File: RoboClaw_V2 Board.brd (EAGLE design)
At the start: 51.8 x 24.4 mm, 11 parts

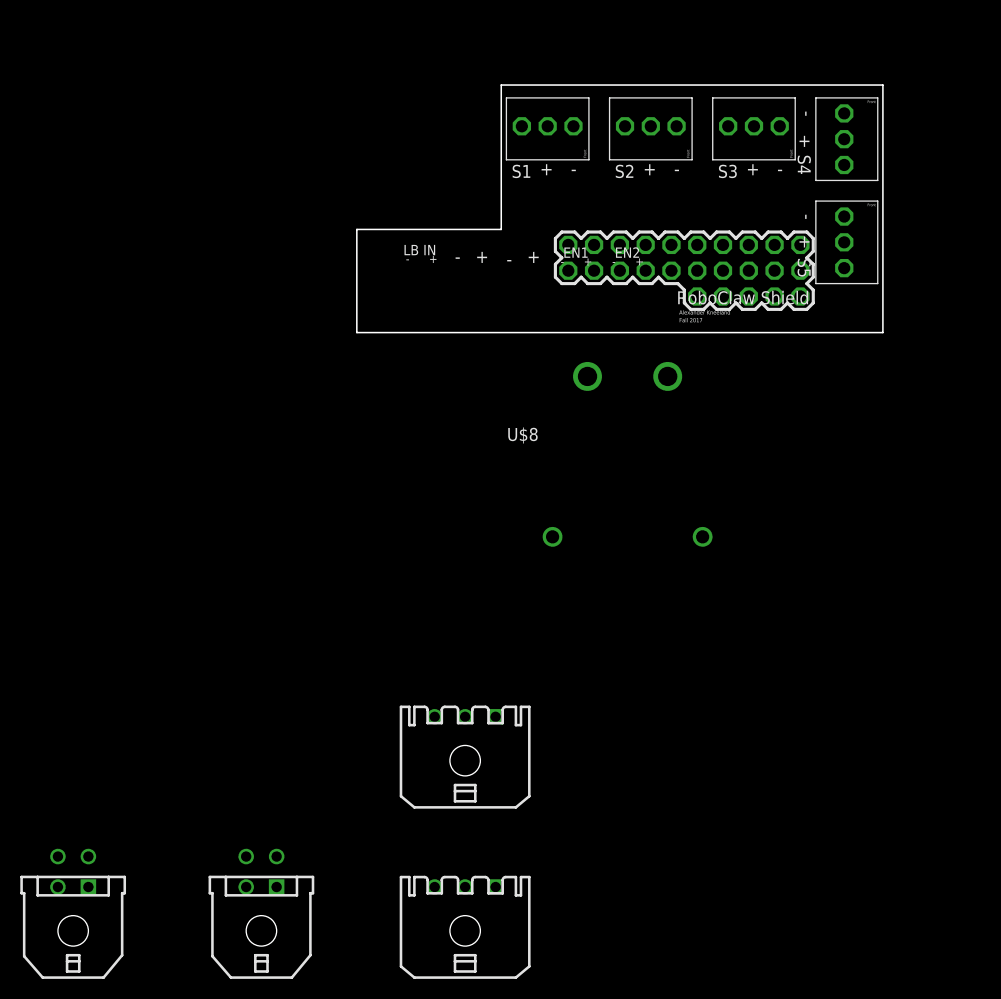
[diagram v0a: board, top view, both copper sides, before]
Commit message: Wired the schematic. Placed and wired the board. First Draft
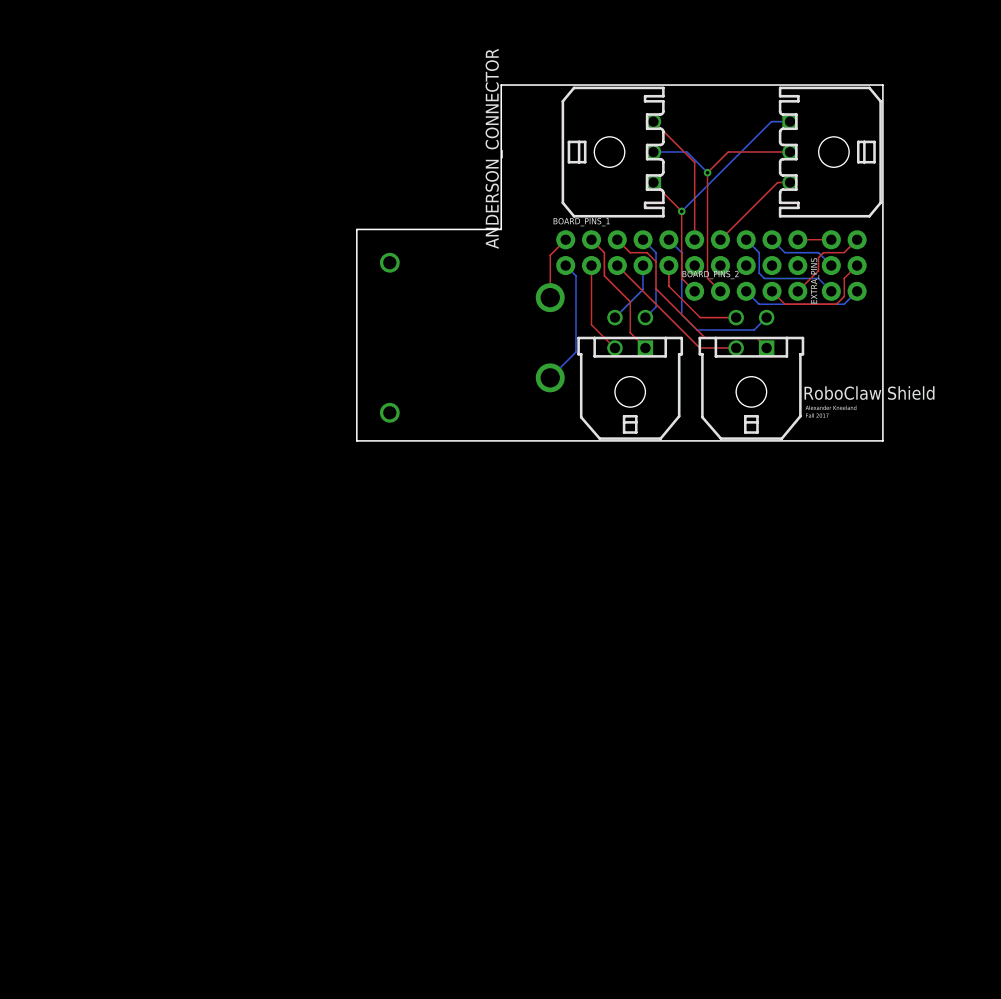
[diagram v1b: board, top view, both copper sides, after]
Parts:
- removed U$1: ROBOCLAW_PINS, Screw Blocks:ROBOCLAW_PINS
- removed U$3, U$4, U$5, U$6, U$7: (no value), Screw Blocks:3_PIN
- removed U$8: (no value), 000_CustomPartsMaster:ANDERSON_RIGHTANGLE_X2
- removed X1, X2: (no value), con-molex-micro-fit-3_0:43650-0300
- removed X3, X4: (no value), con-molex-micro-fit-3_0:43045-0400
- added ANDERSON_CONNECTOR: (no value), 000_CustomPartsMaster:ANDERSON_RIGHTANGLE_X2
- added BOARD_PINS_1: (no value), SparkFun-Connectors:2X10_NOSILK
- added BOARD_PINS_2: (no value), SparkFun-Connectors:1X05_NO_SILK
- added ENCODER_1, ENCODER_2: (no value), con-molex-micro-fit-3_0:43045-0400
- added EXTRA_PINS: (no value), SparkFun-Connectors:2X3-NS
- added RX/TX_IN, RX/TX_OUT: (no value), con-molex-micro-fit-3_0:43650-0300
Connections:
- removed net N$1: U$1.P$17
- removed net N$11: U$1.P$5
- removed net N$12: U$1.P$4
- removed net N$2: U$1.P$19
- removed net N$29: U$1.P$12
- removed net N$3: U$1.P$21
- removed net N$30: U$1.P$11
- removed net N$31: U$1.P$10
- removed net N$32: U$1.P$15
- removed net N$33: U$1.P$14
- removed net N$6: U$4.P$3
- removed net N$7: U$1.P$9
- removed net N$8: U$1.P$8
- removed net N$9: U$1.P$7
- new net EN1_-: BOARD_PINS_1.4, ENCODER_1.P$1
- new net EN1_B: BOARD_PINS_1.8, ENCODER_1.P$3
- new net EN2_-: BOARD_PINS_1.6, ENCODER_2.P$1
- new net EN2_B: BOARD_PINS_1.10, ENCODER_2.P$3
- new net LB_-: ANDERSON_CONNECTOR.P2, BOARD_PINS_1.2
- new net RX(S2): BOARD_PINS_2.2, RX/TX_IN.P$2, RX/TX_OUT.P$2
- new net S1_+: BOARD_PINS_1.11
- new net S1_-: BOARD_PINS_1.12, RX/TX_OUT.P$3
- new net S2_+: BOARD_PINS_1.13
- new net S2_-: BOARD_PINS_1.14, RX/TX_IN.P$3
- new net S3: BOARD_PINS_2.3, EXTRA_PINS.1
- new net S3_+: BOARD_PINS_1.15
- new net S3_-: BOARD_PINS_1.16, EXTRA_PINS.2
- new net S4: BOARD_PINS_2.4, EXTRA_PINS.3
- new net S4_+: BOARD_PINS_1.17
- new net S4_-: BOARD_PINS_1.18, EXTRA_PINS.4
- new net S5: BOARD_PINS_2.5, EXTRA_PINS.5
- new net S5_+: BOARD_PINS_1.19
- new net S5_-: BOARD_PINS_1.20, EXTRA_PINS.6
- new net TX(S1): BOARD_PINS_2.1, RX/TX_IN.P$1, RX/TX_OUT.P$1
- net EN1_+: now also BOARD_PINS_1.3, ENCODER_1.P$2; no longer U$1.P$20
- net EN1_A: now also BOARD_PINS_1.7, ENCODER_1.P$4; no longer U$1.P$18
- net EN2_+: now also BOARD_PINS_1.5, ENCODER_2.P$2; no longer U$1.P$22
- net EN2_A: now also BOARD_PINS_1.9, ENCODER_2.P$4; no longer U$1.P$16
- net LB_+: now also ANDERSON_CONNECTOR.P1, BOARD_PINS_1.1; no longer U$1.P$24
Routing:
- net RX(S2): track 0.00 -> 27.4 mm, vias 0 -> 1
- net TX(S1): track 0.00 -> 26.7 mm, vias 0 -> 1
- net EN2_-: track 0.00 -> 20.7 mm
- net EN2_B: track 0.00 -> 17.4 mm
- net EN2_+: track 0.00 -> 15.1 mm
- net S1_-: track 0.00 -> 13.3 mm
- net EN1_-: track 0.00 -> 12.9 mm
- net LB_+: track 0.00 -> 12.5 mm
- net S3: track 0.00 -> 12.0 mm
- net S3_-: track 0.00 -> 11.7 mm
- net S4: track 0.00 -> 11.5 mm
- net EN2_A: track 0.00 -> 9.94 mm
- net S2_-: track 0.00 -> 9.19 mm
- net EN1_+: track 0.00 -> 9.10 mm
- net S5: track 0.00 -> 8.69 mm
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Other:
- board size 51.8 x 24.4 mm -> 51.8 x 35.1 mm
- board text removed: "+"
- board text removed: "-"
- board text removed: "EN1"
- board text removed: "EN2"
- board text removed: "LB IN"
- board text removed: "S1"
- board text removed: "S2"
- board text removed: "S3"
- board text removed: "S4"
- board text removed: "S5"

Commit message: beefed up connecting wires and moved molex connector to not hit the capacitor on the roboclaw
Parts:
- moved RX/TX_OUT 6.86 mm to (-20.1, 17.8)
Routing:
- net RX(S2): track 27.4 -> 22.4 mm, vias 1 -> 0
- net S1_-: track 13.3 -> 12.8 mm
- net TX(S1): track 26.7 -> 26.5 mm, vias 1 -> 0
